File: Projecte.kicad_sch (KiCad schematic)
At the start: 1 part, among them U1 PIC18F448-IP

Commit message: Update Projecte.kicad_sch
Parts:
- added J1: AudioJack2, symbol Connector_Audio:AudioJack2
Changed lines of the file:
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@@
 	(paper "A4")
+	(symbol
+		(lib_id "Connector_Audio:AudioJack2")
+		(at 238.76 95.25 0)
+		(unit 1)
+		(exclude_from_sim no)
+		(in_bom yes)
+		(on_board yes)
+		(dnp no)
+		(fields_autoplaced yes)
+		(property "Reference" "J1"
+			(at 238.125 86.36 0)
+			(effects
+				(font
+					(size 1.27 1.27)
+				)
+			)
+		)
+		(property "Value" "AudioJack2"
+			(at 238.125 88.9 0)
+			(effects
+				(font
+					(size 1.27 1.27)
+				)
+			)
+		)
+		(property "Footprint" ""
+			(at 238.76 95.25 0)
+			(effects
+				(font
+					(size 1.27 1.27)
+				)
+				(hide yes)
+			)
+		)
+		(property "Datasheet" "~"
+			(at 238.76 95.25 0)
+			(effects
+				(font
+					(size 1.27 1.27)
+				)
+				(hide yes)
+			)
+		)
+		(property "Description" "Audio Jack, 2 Poles (Mono / TS)"
+			(at 238.76 95.25 0)
+			(effects
+				(font
+					(size 1.27 1.27)
+				)
+				(hide yes)
+			)
+		)
+		(pin "S"
+		)
+		(pin "T"
+		)
+		(instances
+			(project ""
+				(path "/3a490218-d26e-483b-a44b-688997a15829"
+					(reference "J1")
+					(unit 1)
+				)
+			)
+		)
+	)
 	(symbol
 		(lib_id "MCU_Microchip_PIC18:PIC18F448-IP")

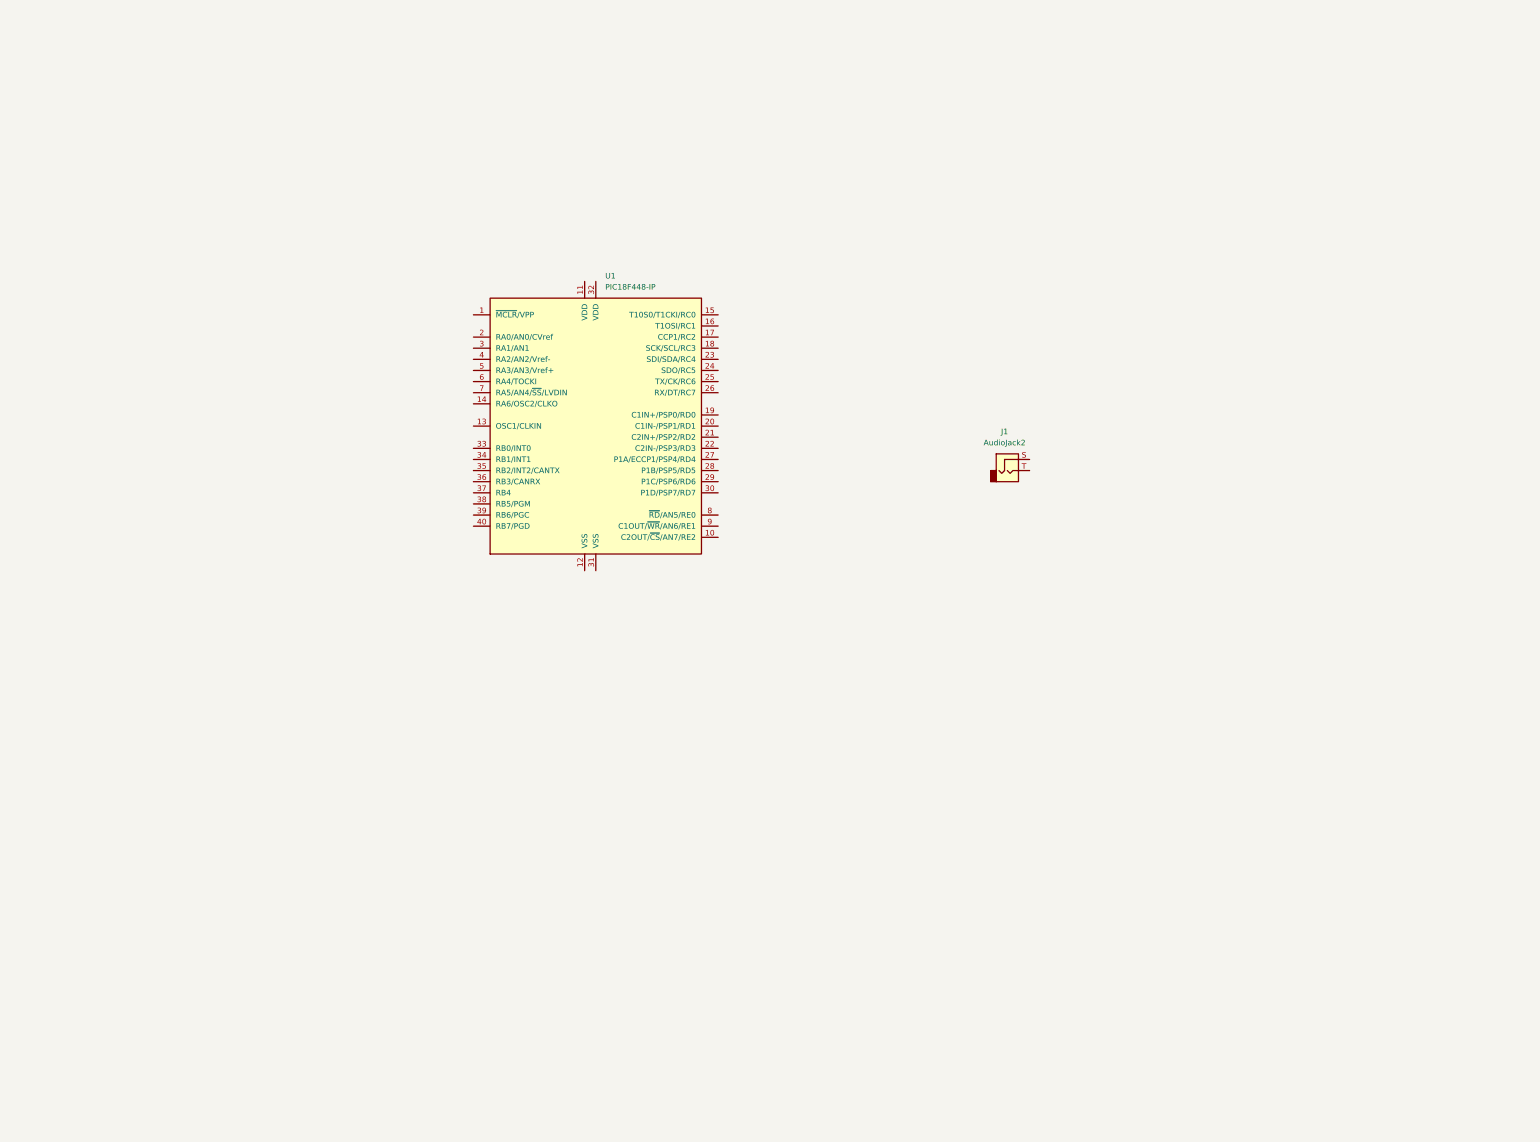
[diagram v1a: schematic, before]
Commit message: Actualització_Esquematic
En el esquematic s'ha afegit el clock, el pont H fet amb mosfets, alguns conectors i el LDO
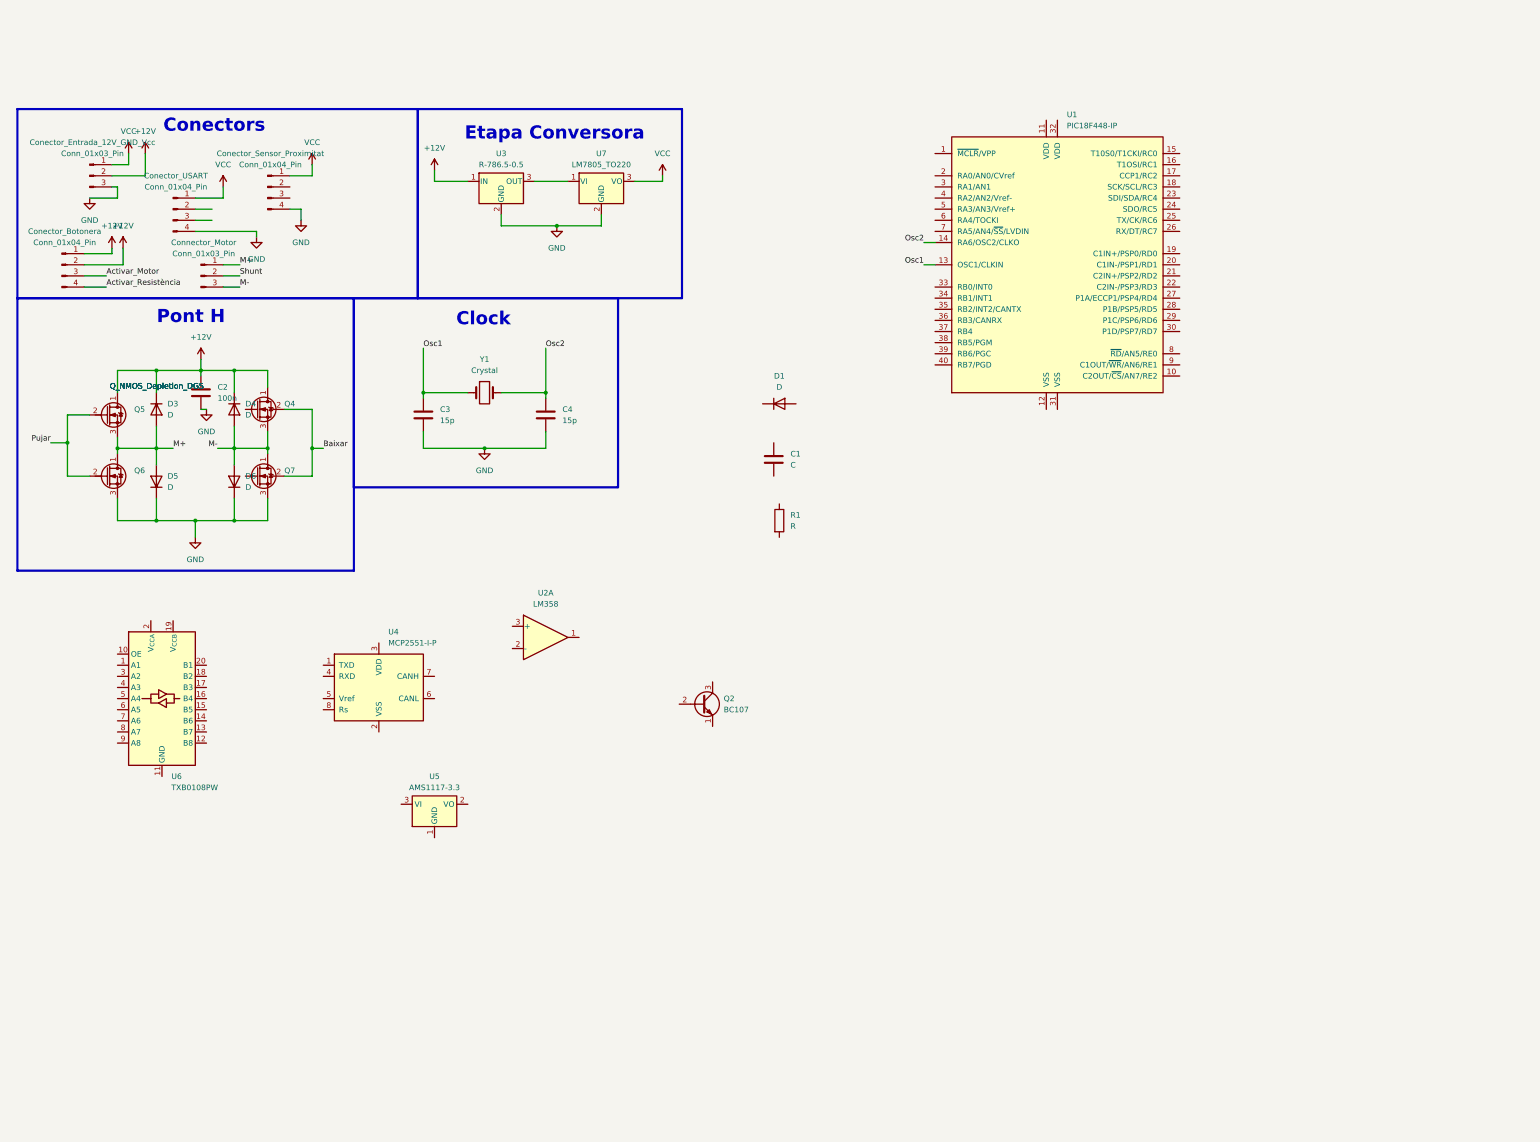
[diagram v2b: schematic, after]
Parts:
- removed J1: AudioJack2, symbol Connector_Audio:AudioJack2
- added C1: C, symbol Device:C
- added C2: 100n, symbol Device:C
- added C3, C4: 15p, symbol Device:C
- added Conector_Botonera, Conector_Sensor_Proximitat, Conector_USART: Conn_01x04_Pin, symbol Connector:Conn_01x04_Pin
- added Conector_Entrada_12V_GND_Vcc, Connector_Motor: Conn_01x03_Pin, symbol Connector:Conn_01x03_Pin
- added D1, D3, D4, D5, D6: D, symbol Device:D
- added Q2: BC107, Package_TO_SOT_THT:TO-18-3, symbol Transistor_BJT:BC107
- added Q4, Q5, Q6, Q7: Q_NMOS_Depletion_DGS, symbol Transistor_FET_Other:Q_NMOS_Depletion_DGS
- added R1: R, symbol Device:R
- added U2: LM358, symbol Amplifier_Operational:LM358
- added U3: R-786.5-0.5, Converter_DCDC:Converter_DCDC_RECOM_R-78E-0.5_THT, symbol Regulator_Switching:R-786.5-0.5
- added U4: MCP2551-I-P, Package_DIP:DIP-8_W7.62mm, symbol Interface_CAN_LIN:MCP2551-I-P
- added U5: AMS1117-3.3, Package_TO_SOT_SMD:SOT-223-3_TabPin2, symbol Regulator_Linear:AMS1117-3.3
- added U6: TXB0108PW, Package_SO:TSSOP-20_4.4x6.5mm_P0.65mm, symbol Logic_LevelTranslator:TXB0108PW
- added U7: LM7805_TO220, Package_TO_SOT_THT:TO-220-3_Vertical, symbol Regulator_Linear:LM7805_TO220
- added Y1: Crystal, symbol Device:Crystal
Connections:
- net Osc1: now reaches U1.13 (OSC1/CLKIN)
- net Osc1: now also C3.1, Y1.1
- net Osc2: now reaches U1.14 (RA6/OSC2/CLKO)
- net Osc2: now also C4.1, Y1.2
- new net: U3.3 (OUT), U7.1 (VI)
- new net +12V: C2.1, Conector_Botonera.1 (Pin_1), Conector_Botonera.2 (Pin_2), Conector_Entrada_12V_GND_Vcc.2 (Pin_2), D3.1 (K), D4.1 (K), Q4.1 (D), Q5.1 (D), U3.1 (IN)
- new net Activar_Motor: Conector_Botonera.3 (Pin_3)
- new net Activar_Resistència: Conector_Botonera.4 (Pin_4)
- new net Baixar: Q4.2 (G), Q7.2 (G)
- new net GND: C2.2, C3.2, C4.2, Conector_Entrada_12V_GND_Vcc.3 (Pin_3), Conector_Sensor_Proximitat.4 (Pin_4), Conector_USART.4 (Pin_4), D5.1 (K), D6.1 (K), Q6.3 (S), Q7.3 (S), U3.2 (GND), U7.2 (GND)
- new net M+: Connector_Motor.1 (Pin_1), D3.2 (A), D5.2 (A), Q5.3 (S), Q6.1 (D)
- new net M-: Connector_Motor.3 (Pin_3), D4.2 (A), D6.2 (A), Q4.3 (S), Q7.1 (D)
- new net Pujar: Q5.2 (G), Q6.2 (G)
- new net Shunt: Connector_Motor.2 (Pin_2)
- new net VCC: Conector_Entrada_12V_GND_Vcc.1 (Pin_1), Conector_Sensor_Proximitat.1 (Pin_1), Conector_USART.1 (Pin_1), U7.3 (VO)
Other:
- note added: "Clock"
- note added: "Conectors"
- note added: "Etapa Conversora"
- note added: "Pont H"
- moved on the sheet: U1

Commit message: Otra
He afeguit el transciver, i estic fent el programming del xip, no tinc molt clar si esta bé pero working on it si vols fer tu els sensors de lokos.
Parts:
- removed Q4, Q5, Q6, Q7: Q_NMOS_Depletion_DGS, symbol Transistor_FET_Other:Q_NMOS_Depletion_DGS
- added C5: 100N, symbol Device:C
- added ConnectorCAN1: DE9_Pins, Connector_Dsub:DSUB-9_Pins_Horizontal_P2.77x2.84mm_EdgePinOffset4.94mm_Housed_MountingHolesOffset4.94mm, symbol Connector:DE9_Pins
- added DB1: LED, LED_SMD:LED_0805_2012Metric_Pad1.15x1.40mm_HandSolder, symbol Device:LED
- added DR1: LED, LED_SMD:LED_0805_2012Metric, symbol Device:LED
- added J_MCLR1: Conn_01x03, Connector_PinHeader_2.54mm:PinHeader_1x03_P2.54mm_Vertical, symbol Connector_Generic:Conn_01x03
- added J_Programació: Conn_01x06_Pin, symbol Connector:Conn_01x06_Pin
- added Q1, Q3, Q4, Q5, Q6: IRLZ34N, Package_TO_SOT_THT:TO-220-3_Vertical, symbol Transistor_FET:IRLZ34N
- added R2, R3, R4: 1k, symbol Device:R
- added R5: 200, Resistor_SMD:R_0805_2012Metric, symbol Device:R
- added R6: R, Resistor_SMD:R_0805_2012Metric, symbol Device:R
- added RMCLR: 1k, Resistor_SMD:R_0805_2012Metric, symbol Device:R
- added SW_MCLR1: SW_Push, Button_Switch_THT:SW_PUSH_6mm, symbol Switch:SW_Push
- renumbered Conector_Botonera to Conector_Botonera1, Conector_Entrada_12V_GND_Vcc to Conector_Entrada_12V_GND_Vcc1, Conector_Sensor_Proximitat to Conector_Sensor_Proximitat1, Conector_USART to Conector_USART1, Connector_Motor to Connector_Motor1
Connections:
- net +12V: now also Q1.2 (D), Q4.2 (D)
- net Baixar: now also Q1.1 (G), Q5.1 (G)
- net GND: now also U1.12 (VSS), U1.31 (VSS), U4.2 (VSS), C5.2, ConnectorCAN1.3, ConnectorCAN1.6, DB1.1 (K), DR1.1 (K), J_Programació.6 (Pin_6), Q3.3 (S), Q5.3 (S), R3.2, R4.1, SW_MCLR1.2
- net M+: now also Q4.3 (S), Q5.2 (D)
- net M-: now also Q1.3 (S), Q3.2 (D)
- net Pujar: now also Q3.1 (G), Q4.1 (G)
- net VCC: now also U1.11 (VDD), U1.32 (VDD), U4.3 (VDD), C5.1, ConnectorCAN1.9, J_Programació.2 (Pin_2), Q6.2 (D), R2.1, R5.2, RMCLR.2
- net MCLR: now reaches U1.1 (~{MCLR}/VPP)
- net MCLR: now also J_MCLR1.1 (Pin_1)
- net Tx: now reaches U1.35 (RB2/INT2/CANTX)
- net Tx: now also U4.1 (TXD)
- net Rx: now reaches U1.36 (RB3/CANRX)
- net Rx: now also U4.4 (RXD)
- net PGM: now reaches U1.38 (RB5/PGM)
- net PGM: now also Q6.3 (S), R6.2
- net Vref: now reaches U4.5 (Vref)
- net Vref: now also R2.2, R3.1
- net Canl: now reaches U4.6 (CANL)
- net Canl: now also ConnectorCAN1.2
- net Canh: now reaches U4.7 (CANH)
- net Canh: now also ConnectorCAN1.7
- net at U4.8 (Rs): now also R4.2
- new net: DB1.2 (A), R5.1
- new net: DR1.2 (A), R6.1
- new net: J_MCLR1.2 (Pin_2), RMCLR.1, SW_MCLR1.1
- new net: J_MCLR1.3 (Pin_3), J_Programació.5 (Pin_5)
- new net PGC: J_Programació.3 (Pin_3)
- new net PGD: J_Programació.4 (Pin_4)
- new net Program_Enable: J_Programació.1 (Pin_1), Q6.1 (G)
- no-connect marks 0 -> 4
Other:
- note added: "BUS CAN"
- note added: "Clk a 4Mhz"
- note added: "Imáx=1,5A"
- note added: "Programació Xip"
- note added: "Un 1 en la senyal pujar fa girar el motor en sentit horari mentres que un 1 en la senyal baixar fa el contrari pujar=not(baixar)"
- note added: "Vale en pel que he estat mirant PGM es la senyal per activar la programació, quan al pin 38 se li aplica Vdd s'activa el progamming mode, llavors jo he ficat el mosfet per a poder enviar vcc amb una senyal externa program enable"
- note added: "Vcc=5V"
- company: (none) -> UB
- title: (none) -> Projecte_v1
- moved on the sheet: C1, Conector_Entrada_12V_GND_Vcc1, Connector_Motor1, D1, Q2, R1, U1, U2A, U4, U5, U6
